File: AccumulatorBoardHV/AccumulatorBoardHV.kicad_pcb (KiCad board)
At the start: 2 copper layers, 179.7 x 69.2 mm, 48 parts, among them J1 TS -> GLV Regulator Jumper, J10 Charger Current, J2 To LV Board, J3 Batt Voltage, J4 TS (Switched), J5 IMD TS, J6 To LV Board, J7 Acc LED 1, J8 Acc LED 2, J9 Charger Current to Batt, U1 V110C12E100BL, U2 DK1A1B-12V, U3 RDD08110S3V3, U4 PS2501-4, U5 G2RL-1A-E, U6 G2RL-1A-E

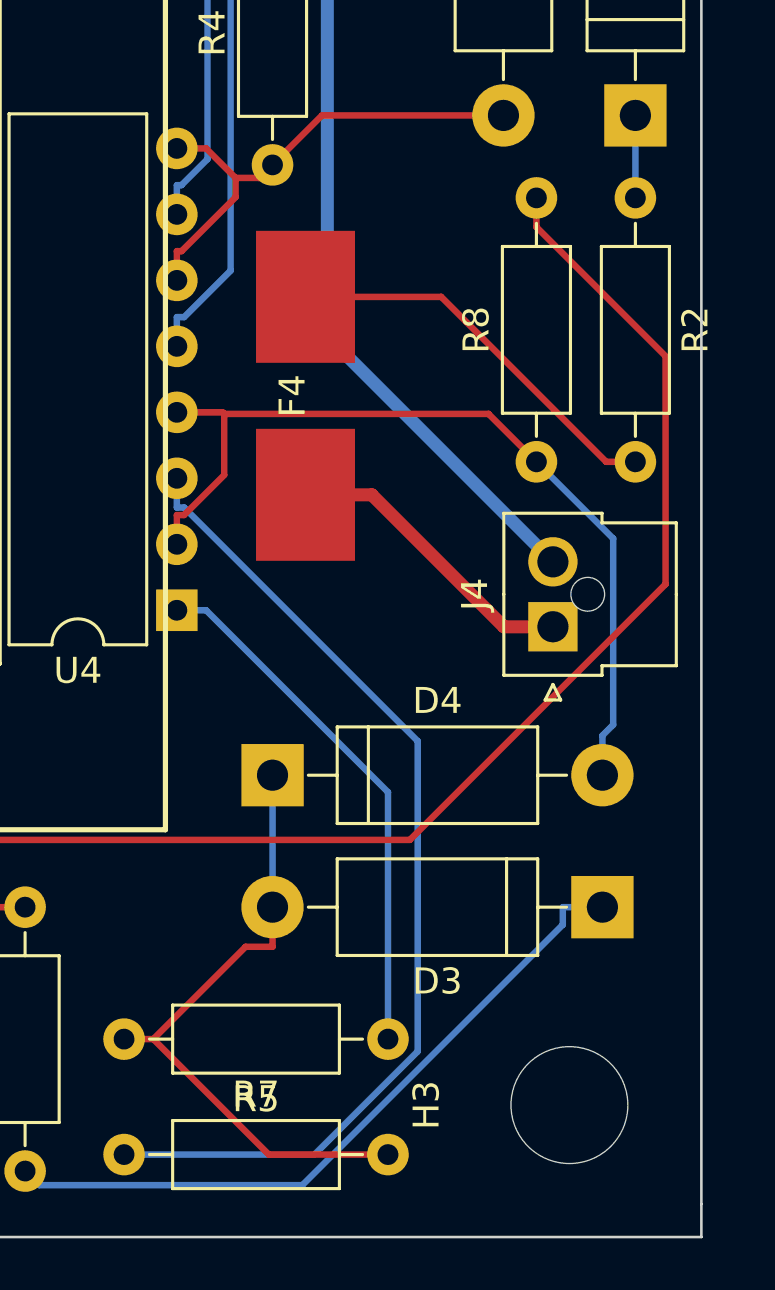
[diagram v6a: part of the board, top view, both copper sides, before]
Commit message: Tweak routing on boards, add mounting holes to dash switchbox
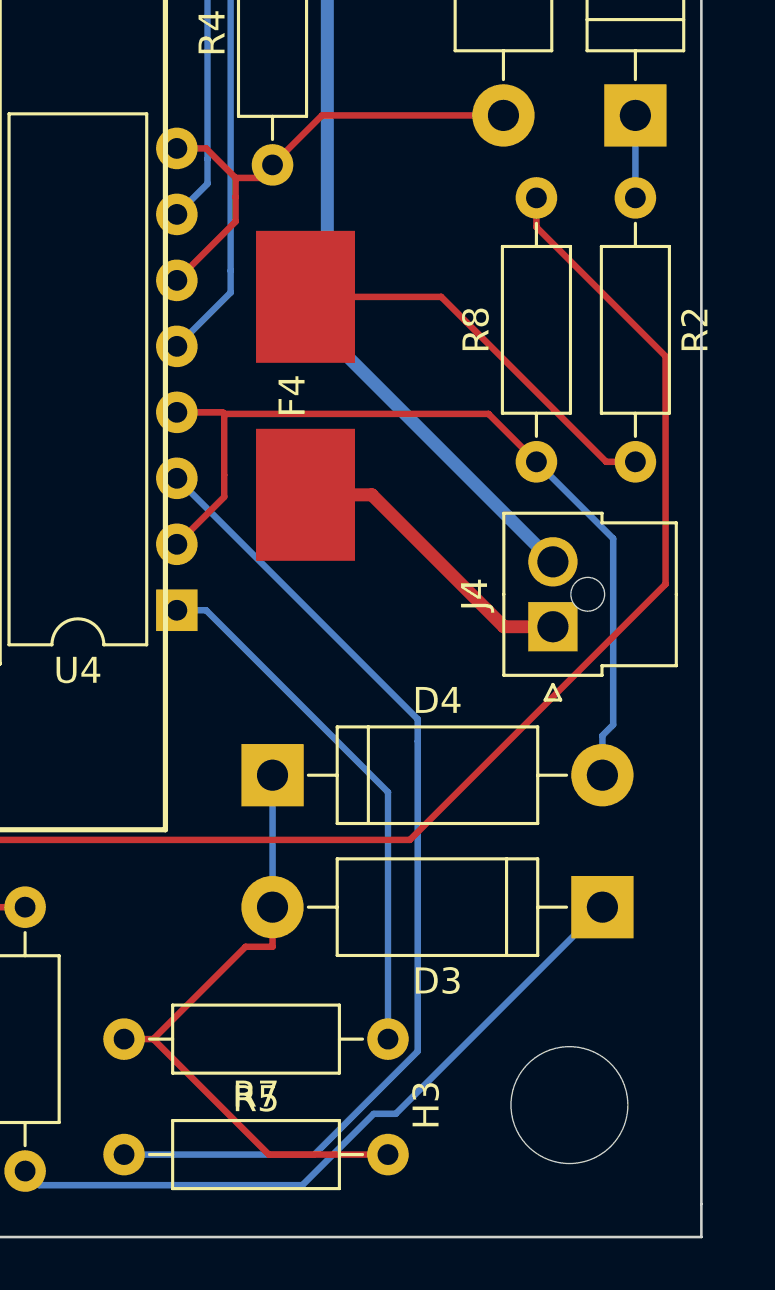
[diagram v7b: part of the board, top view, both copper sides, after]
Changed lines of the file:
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@@
     (thickness 1.6)
     (drawings 15)
-    (tracks 269)
+    (tracks 264)
     (zones 0)
     (modules 48)
@@
   (segment (start 195.58 44.45) (end 195.58 42.9247) (width 0.25) (layer B.Cu) (net 8))
   (segment (start 190.5 35.56) (end 186.69 35.56) (width 0.25) (layer F.Cu) (net 8))
-  (segment (start 183.007 63.5) (end 183.007 62.3747) (width 0.25) (layer F.Cu) (net 9))
+  (segment (start 185.2697 60.2936) (end 185.2697 61.2373) (width 0.25) (layer F.Cu) (net 9))
+  (segment (start 185.2697 61.2373) (end 183.007 63.5) (width 0.25) (layer F.Cu) (net 9) (status 800000))
   (segment (start 188.595 57.15) (end 186.69 59.055) (width 0.25) (layer F.Cu) (net 9))
   (segment (start 195.58 57.15) (end 188.595 57.15) (width 0.25) (layer F.Cu) (net 9))
   (segment (start 183.007 58.42) (end 184.1323 58.42) (width 0.25) (layer F.Cu) (net 9))
-  (segment (start 183.1886 62.3747) (end 183.007 62.3747) (width 0.25) (layer F.Cu) (net 9))
-  (segment (start 185.2697 60.2936) (end 183.1886 62.3747) (width 0.25) (layer F.Cu) (net 9))
   (segment (start 185.2697 59.5574) (end 185.2697 60.2936) (width 0.25) (layer F.Cu) (net 9))
   (segment (start 186.1876 59.5574) (end 185.2697 59.5574) (width 0.25) (layer F.Cu) (net 9))
   (segment (start 186.69 59.055) (end 186.1876 59.5574) (width 0.25) (layer F.Cu) (net 9))
   (segment (start 185.2697 59.5574) (end 184.1323 58.42) (width 0.25) (layer F.Cu) (net 9))
+  (segment (start 190.5839 95.5879) (end 191.4321 95.5879) (width 0.25) (layer B.Cu) (net 10))
+  (segment (start 191.4321 95.5879) (end 199.39 87.63) (width 0.25) (layer B.Cu) (net 10) (status 800000))
   (segment (start 177.7069 98.3319) (end 177.165 97.79) (width 0.25) (layer B.Cu) (net 10))
   (segment (start 187.8399 98.3319) (end 177.7069 98.3319) (width 0.25) (layer B.Cu) (net 10))
-  (segment (start 197.8647 88.3071) (end 187.8399 98.3319) (width 0.25) (layer B.Cu) (net 10))
-  (segment (start 197.8647 87.63) (end 197.8647 88.3071) (width 0.25) (layer B.Cu) (net 10))
-  (segment (start 199.39 87.63) (end 197.8647 87.63) (width 0.25) (layer B.Cu) (net 10))
+  (segment (start 190.5839 95.5879) (end 187.8399 98.3319) (width 0.25) (layer B.Cu) (net 10))
   (segment (start 186.69 82.55) (end 186.69 87.63) (width 0.25) (layer B.Cu) (net 11))
   (segment (start 186.5453 97.155) (end 191.135 97.155) (width 0.25) (layer F.Cu) (net 11))
@@
   (segment (start 186.69 89.1553) (end 185.655 89.1553) (width 0.25) (layer F.Cu) (net 11))
   (segment (start 186.69 87.63) (end 186.69 89.1553) (width 0.25) (layer F.Cu) (net 11))
+  (segment (start 184.831 70.992) (end 184.831 71.836) (width 0.25) (layer F.Cu) (net 12))
+  (segment (start 184.831 71.836) (end 183.007 73.66) (width 0.25) (layer F.Cu) (net 12) (status 800000))
   (segment (start 199.8048 73.4398) (end 196.85 70.485) (width 0.25) (layer B.Cu) (net 12))
   (segment (start 199.8048 80.6099) (end 199.8048 73.4398) (width 0.25) (layer B.Cu) (net 12))
   (segment (start 199.39 81.0247) (end 199.8048 80.6099) (width 0.25) (layer B.Cu) (net 12))
   (segment (start 199.39 82.55) (end 199.39 81.0247) (width 0.25) (layer B.Cu) (net 12))
-  (segment (start 183.007 73.66) (end 183.007 72.5347) (width 0.25) (layer F.Cu) (net 12))
   (segment (start 195.0045 68.6395) (end 184.831 68.6395) (width 0.25) (layer F.Cu) (net 12))
   (segment (start 196.85 70.485) (end 195.0045 68.6395) (width 0.25) (layer F.Cu) (net 12))
   (segment (start 184.7715 68.58) (end 184.831 68.6395) (width 0.25) (layer F.Cu) (net 12))
   (segment (start 183.007 68.58) (end 184.7715 68.58) (width 0.25) (layer F.Cu) (net 12))
-  (segment (start 183.2883 72.5347) (end 183.007 72.5347) (width 0.25) (layer F.Cu) (net 12))
-  (segment (start 184.831 70.992) (end 183.2883 72.5347) (width 0.25) (layer F.Cu) (net 12))
   (segment (start 184.831 68.6395) (end 184.831 70.992) (width 0.25) (layer F.Cu) (net 12))
   (segment (start 168.91 92.0903) (end 170.18 90.8203) (width 0.5) (layer F.Cu) (net 13))
@@
   (segment (start 62.3824 56.9604) (end 71.5576 56.9604) (width 4) (layer F.Cu) (net 22))
   (segment (start 71.561 56.957) (end 71.561 61.957) (width 4) (layer B.Cu) (net 22))
-  (segment (start 183.2883 64.9147) (end 183.007 64.9147) (width 0.25) (layer B.Cu) (net 23))
-  (segment (start 185.0785 63.1245) (end 183.2883 64.9147) (width 0.25) (layer B.Cu) (net 23))
+  (segment (start 185.0785 63.1245) (end 185.0785 63.9685) (width 0.25) (layer B.Cu) (net 23))
+  (segment (start 185.0785 63.9685) (end 183.007 66.04) (width 0.25) (layer B.Cu) (net 23) (status 800000))
   (segment (start 185.0785 48.5938) (end 185.0785 63.1245) (width 0.25) (layer B.Cu) (net 23))
   (segment (start 186.5063 47.166) (end 185.0785 48.5938) (width 0.25) (layer B.Cu) (net 23))
   (segment (start 189.054 47.166) (end 186.5063 47.166) (width 0.25) (layer B.Cu) (net 23))
   (segment (start 190.5 45.72) (end 189.054 47.166) (width 0.25) (layer B.Cu) (net 23))
-  (segment (start 183.007 66.04) (end 183.007 64.9147) (width 0.25) (layer B.Cu) (net 23))
-  (segment (start 183.1839 59.8347) (end 183.007 59.8347) (width 0.25) (layer B.Cu) (net 24))
-  (segment (start 184.1873 58.8313) (end 183.1839 59.8347) (width 0.25) (layer B.Cu) (net 24))
+  (segment (start 184.1873 58.8313) (end 184.1873 59.7797) (width 0.25) (layer B.Cu) (net 24))
+  (segment (start 184.1873 59.7797) (end 183.007 60.96) (width 0.25) (layer B.Cu) (net 24) (status 800000))
   (segment (start 184.1873 48.2227) (end 184.1873 58.8313) (width 0.25) (layer B.Cu) (net 24))
   (segment (start 186.69 45.72) (end 184.1873 48.2227) (width 0.25) (layer B.Cu) (net 24))
-  (segment (start 183.007 60.96) (end 183.007 59.8347) (width 0.25) (layer B.Cu) (net 24))
   (segment (start 191.135 83.2027) (end 184.1323 76.2) (width 0.25) (layer B.Cu) (net 25))
   (segment (start 191.135 92.71) (end 191.135 83.2027) (width 0.25) (layer B.Cu) (net 25))
   (segment (start 183.007 76.2) (end 184.1323 76.2) (width 0.25) (layer B.Cu) (net 25))
-  (segment (start 183.2883 72.2453) (end 183.007 72.2453) (width 0.25) (layer B.Cu) (net 26))
-  (segment (start 192.2799 81.2369) (end 183.2883 72.2453) (width 0.25) (layer B.Cu) (net 26))
+  (segment (start 192.2799 81.2369) (end 192.2799 80.3929) (width 0.25) (layer B.Cu) (net 26))
+  (segment (start 192.2799 80.3929) (end 183.007 71.12) (width 0.25) (layer B.Cu) (net 26) (status 800000))
   (segment (start 192.2799 93.1816) (end 192.2799 81.2369) (width 0.25) (layer B.Cu) (net 26))
   (segment (start 188.3065 97.155) (end 192.2799 93.1816) (width 0.25) (layer B.Cu) (net 26))
   (segment (start 180.975 97.155) (end 188.3065 97.155) (width 0.25) (layer B.Cu) (net 26))
-  (segment (start 183.007 71.12) (end 183.007 72.2453) (width 0.25) (layer B.Cu) (net 26))
   (segment (start 53.34 94.615) (end 45.72 94.615) (width 0.5) (layer F.Cu) (net 27))
   (segment (start 83.82 85.725) (end 101.6 85.725) (width 0.5) (layer F.Cu) (net 28))
